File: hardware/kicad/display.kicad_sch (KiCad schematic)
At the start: 0 parts

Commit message: first pass schematic and new fpc symbol
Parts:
- added C31, C32, C33, C34, C35, C36, C37, C38, C39, C40: 1u, symbol Device:C_Small
- added C41: 4.7u, symbol Device:C_Small
- added D4, D5, D6: MBR0530, Diode_SMD:D_SOD-123, symbol Diode:MBR0530
- added L5: 10u 1A, symbol Device:L
- added Q7: SI1308EDL, Package_TO_SOT_SMD:SOT-23, symbol Transistor_FET:AO3400A
- added R17: 0.47, Resistor_SMD:R_0402_1005Metric, symbol Device:R_Small
- added R17: 1M, Resistor_SMD:R_0402_1005Metric, symbol Device:R_Small
- added U8: FPC-05FB-24PH20, symbol plantpal:GDEW0154M10
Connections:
- new net: C32.2, U8.5 (VGH)
- new net: C38.2, U8.24 (VCOM)
- new net: C34.2, U8.18 (VDD)
- new net: C41.2, D6.2 (A), L5.2, Q7.3 (D)
- new net: C36.2, U8.22 (VSL)
- new net: C35.2, U8.20 (VSH)
- new net: C41.1, D4.1 (K), D5.2 (A)
- new net: C31.1, U8.4 (VGL)
- new net +3V3: C33.2, C40.1, L5.1, U8.15 (VDDIO), U8.16 (VCI)
- new net BUSY: U8.9 (BUSY)
- new net CS: U8.12 (CS)
- new net DC: U8.11 (D/C)
- new net GDR: Q7.1 (G), R17.2, U8.2 (GDR)
- new net GND: C31.2, C32.1, C33.1, C34.1, C35.1, C36.1, C37.1, C38.1, C39.1, C40.2, D5.1 (K), R17.1, R17.1, U8.17 (VSS), U8.8 (BS1)
- new net PREVGH: C39.2, D6.1 (K), U8.21 (PREVGH)
- new net PREVGL: C37.2, D4.2 (A), U8.23 (PREVGL)
- new net RESE: Q7.2 (S), R17.2, U8.3 (RESE)
- new net RST: U8.10 (RST)
- new net SCLK: U8.13 (SCLK)
- new net SDI: U8.14 (SDI)
- new net TSCL: U8.6 (TSCL)
- new net TSDA: U8.7 (TSDA)
- no-connect marks 0 -> 1
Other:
- note added: "Display Manufacturer: Good Display Part Number: GDEW0154I9FC 26Pin FPC, 0.5mm Pitch, 0.25mm Pad Size Pin 1 and 26 are not used No connector is need, soldered directly to board Use 24 pin FPC connector footprint for debugging"
- note added: "E-Paper Display"
- note added: "Sheets Connection"

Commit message: clean-up
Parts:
- C41: value 4.7u -> 4u7
- renumbered C34 to C32, C38 to C33, C36 to C34, C37 to C36, C31 to C37, C32 to C38, C33 to C39, C39 to C40, C40 to C42, U8 to J4
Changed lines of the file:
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@@
   (symbol (lib_id "Device:C_Small") (at 64.77 38.735 270) (mirror x) (unit 1)
     (in_bom yes) (on_board yes) (dnp no)
-    (property "Reference" "C32" (at 66.04 41.275 90)
+    (property "Reference" "C38" (at 66.04 41.275 90)
       (effects (font (size 1.27 1.27)) (justify left))
     )
@@
       (project "plantpal"
         (path "/59b4123e-c7be-466b-a5db-658b8f0c1171/3265fc00-478b-4188-a908-4fc9b1aaf6ab"
-          (reference "C32") (unit 1)
+          (reference "C38") (unit 1)
         )
       )
@@
   (symbol (lib_id "Device:C_Small") (at 55.88 109.855 270) (unit 1)
     (in_bom yes) (on_board yes) (dnp no)
-    (property "Reference" "C38" (at 57.15 108.585 90)
+    (property "Reference" "C33" (at 57.15 108.585 90)
       (effects (font (size 1.27 1.27)) (justify left))
     )
@@
       (project "plantpal"
         (path "/59b4123e-c7be-466b-a5db-658b8f0c1171/3265fc00-478b-4188-a908-4fc9b1aaf6ab"
-          (reference "C38") (unit 1)
+          (reference "C33") (unit 1)
         )
       )
@@
         )
         (path "/59b4123e-c7be-466b-a5db-658b8f0c1171/3265fc00-478b-4188-a908-4fc9b1aaf6ab"
-          (reference "#PWR089") (unit 1)
+          (reference "#PWR0102") (unit 1)
         )
       )
@@
   (symbol (lib_id "power:GND") (at 69.85 113.665 0) (mirror y) (unit 1)
     (in_bom yes) (on_board yes) (dnp no) (fields_autoplaced)
-    (property "Reference" "#PWR092" (at 69.85 120.015 0)
+    (property "Reference" "#PWR095" (at 69.85 120.015 0)
       (effects (font (size 1.27 1.27)) hide)
     )
@@
       (project "plantpal"
         (path "/59b4123e-c7be-466b-a5db-658b8f0c1171/3265fc00-478b-4188-a908-4fc9b1aaf6ab"
-          (reference "#PWR092") (unit 1)
+          (reference "#PWR095") (unit 1)
         )
       )
@@
         )
         (path "/59b4123e-c7be-466b-a5db-658b8f0c1171/3265fc00-478b-4188-a908-4fc9b1aaf6ab"
-          (reference "R26") (unit 1)
+          (reference "R25") (unit 1)
         )
       )
@@
         )
         (path "/59b4123e-c7be-466b-a5db-658b8f0c1171/3265fc00-478b-4188-a908-4fc9b1aaf6ab"
-          (reference "#PWR091") (unit 1)
+          (reference "#PWR094") (unit 1)
         )
       )
@@
   (symbol (lib_id "Device:C_Small") (at 177.8 59.055 0) (mirror y) (unit 1)
     (in_bom yes) (on_board yes) (dnp no)
-    (property "Reference" "C40" (at 175.26 57.15 0)
+    (property "Reference" "C42" (at 175.26 57.15 0)
       (effects (font (size 1.27 1.27)) (justify left))
     )
@@
       (project "plantpal"
         (path "/59b4123e-c7be-466b-a5db-658b8f0c1171/3265fc00-478b-4188-a908-4fc9b1aaf6ab"
-          (reference "C40") (unit 1)
+          (reference "C42") (unit 1)
         )
       )
@@
   (symbol (lib_id "Device:C_Small") (at 54.61 86.995 270) (unit 1)
     (in_bom yes) (on_board yes) (dnp no)
-    (property "Reference" "C34" (at 55.88 85.725 90)
+    (property "Reference" "C32" (at 55.88 85.725 90)
       (effects (font (size 1.27 1.27)) (justify left))
     )
@@
       (project "plantpal"
         (path "/59b4123e-c7be-466b-a5db-658b8f0c1171/3265fc00-478b-4188-a908-4fc9b1aaf6ab"
-          (reference "C34") (unit 1)
+          (reference "C32") (unit 1)
         )
       )
@@
   (symbol (lib_id "power:GND") (at 177.8 65.405 0) (mirror y) (unit 1)
     (in_bom yes) (on_board yes) (dnp no) (fields_autoplaced)
-    (property "Reference" "#PWR097" (at 177.8 71.755 0)
+    (property "Reference" "#PWR0101" (at 177.8 71.755 0)
       (effects (font (size 1.27 1.27)) hide)
     )
@@
       (project "plantpal"
         (path "/59b4123e-c7be-466b-a5db-658b8f0c1171/3265fc00-478b-4188-a908-4fc9b1aaf6ab"
-          (reference "#PWR097") (unit 1)
+          (reference "#PWR0101") (unit 1)
         )
       )
@@
   (symbol (lib_id "Device:C_Small") (at 63.5 106.045 270) (unit 1)
     (in_bom yes) (on_board yes) (dnp no)
-    (property "Reference" "C37" (at 64.77 104.775 90)
+    (property "Reference" "C36" (at 64.77 104.775 90)
       (effects (font (size 1.27 1.27)) (justify left))
     )
@@
       (project "plantpal"
         (path "/59b4123e-c7be-466b-a5db-658b8f0c1171/3265fc00-478b-4188-a908-4fc9b1aaf6ab"
-          (reference "C37") (unit 1)
+          (reference "C36") (unit 1)
         )
       )
@@
   (symbol (lib_id "Device:C_Small") (at 109.22 61.595 0) (mirror x) (unit 1)
     (in_bom yes) (on_board yes) (dnp no)
-    (property "Reference" "C39" (at 102.87 59.055 0)
+    (property "Reference" "C40" (at 102.87 59.055 0)
       (effects (font (size 1.27 1.27)) (justify left))
     )
@@
       (project "plantpal"
         (path "/59b4123e-c7be-466b-a5db-658b8f0c1171/3265fc00-478b-4188-a908-4fc9b1aaf6ab"
-          (reference "C39") (unit 1)
+          (reference "C40") (unit 1)
         )
       )
@@
   (symbol (lib_id "Device:C_Small") (at 57.15 102.235 270) (unit 1)
     (in_bom yes) (on_board yes) (dnp no)
-    (property "Reference" "C36" (at 58.42 100.965 90)
+    (property "Reference" "C34" (at 58.42 100.965 90)
       (effects (font (size 1.27 1.27)) (justify left))
     )
@@
       (project "plantpal"
         (path "/59b4123e-c7be-466b-a5db-658b8f0c1171/3265fc00-478b-4188-a908-4fc9b1aaf6ab"
-          (reference "C36") (unit 1)
+          (reference "C34") (unit 1)
         )
       )
@@
   (symbol (lib_id "power:GND") (at 146.05 80.645 0) (mirror y) (unit 1)
     (in_bom yes) (on_board yes) (dnp no) (fields_autoplaced)
-    (property "Reference" "#PWR095" (at 146.05 86.995 0)
+    (property "Reference" "#PWR099" (at 146.05 86.995 0)
       (effects (font (size 1.27 1.27)) hide)
     )
@@
       (project "plantpal"
         (path "/59b4123e-c7be-466b-a5db-658b8f0c1171/3265fc00-478b-4188-a908-4fc9b1aaf6ab"
-          (reference "#PWR095") (unit 1)
+          (reference "#PWR099") (unit 1)
         )
       )
@@
   (symbol (lib_id "power:GND") (at 74.93 45.085 0) (mirror y) (unit 1)
     (in_bom yes) (on_board yes) (dnp no) (fields_autoplaced)
-    (property "Reference" "#PWR090" (at 74.93 51.435 0)
+    (property "Reference" "#PWR096" (at 74.93 51.435 0)
       (effects (font (size 1.27 1.27)) hide)
     )
@@
       (project "plantpal"
         (path "/59b4123e-c7be-466b-a5db-658b8f0c1171/3265fc00-478b-4188-a908-4fc9b1aaf6ab"
-          (reference "#PWR090") (unit 1)
+          (reference "#PWR096") (unit 1)
         )
       )
@@
       (effects (font (size 1.27 1.27)) (justify left))
     )
-    (property "Value" "4.7u" (at 132.715 48.26 0)
+    (property "Value" "4u7" (at 132.715 48.26 0)
       (effects (font (size 1.27 1.27)) (justify left))
     )
@@
         )
         (path "/59b4123e-c7be-466b-a5db-658b8f0c1171/3265fc00-478b-4188-a908-4fc9b1aaf6ab"
-          (reference "#PWR096") (unit 1)
+          (reference "#PWR0100") (unit 1)
         )
       )
@@
         )
         (path "/59b4123e-c7be-466b-a5db-658b8f0c1171/3265fc00-478b-4188-a908-4fc9b1aaf6ab"
-          (reference "R25") (unit 1)
+          (reference "R26") (unit 1)
         )
       )
@@
   (symbol (lib_id "Device:C_Small") (at 69.85 79.375 180) (unit 1)
     (in_bom yes) (on_board yes) (dnp no)
-    (property "Reference" "C33" (at 76.2 76.835 0)
+    (property "Reference" "C39" (at 76.2 76.835 0)
       (effects (font (size 1.27 1.27)) (justify left))
     )
@@
       (project "plantpal"
         (path "/59b4123e-c7be-466b-a5db-658b8f0c1171/3265fc00-478b-4188-a908-4fc9b1aaf6ab"
-          (reference "C33") (unit 1)
+          (reference "C39") (unit 1)
         )
       )
@@
   (symbol (lib_id "plantpal:GDEW0154M10") (at 34.29 62.865 0) (mirror y) (unit 1)
     (in_bom yes) (on_board yes) (dnp no)
-    (property "Reference" "U8" (at 26.67 116.84 0)
+    (property "Reference" "J4" (at 26.67 116.84 0)
       (effects (font (size 1.27 1.27)) (justify left))
     )
@@
     )
     (property "Part Number" "FPC-05FB-24PH20" (at 34.29 62.865 0)
+      (effects (font (size 1.27 1.27)) hide)
+    )
+    (property "Part Description" "" (at 34.29 62.865 0)
+      (effects (font (size 1.27 1.27)) hide)
+    )
+    (property "Manufacturer Part Number" "" (at 34.29 62.865 0)
+      (effects (font (size 1.27 1.27)) hide)
+    )
+    (property "Distributor" "" (at 34.29 62.865 0)
+      (effects (font (size 1.27 1.27)) hide)
+    )
+    (property "Distributor Part Number" "" (at 34.29 62.865 0)
+      (effects (font (size 1.27 1.27)) hide)
+    )
+    (property "Distributor Link" "" (at 34.29 62.865 0)
       (effects (font (size 1.27 1.27)) hide)
     )
@@
       (project "plantpal"
         (path "/59b4123e-c7be-466b-a5db-658b8f0c1171/3265fc00-478b-4188-a908-4fc9b1aaf6ab"
-          (reference "U8") (unit 1)
+          (reference "J4") (unit 1)
         )
       )
@@
   (symbol (lib_id "power:GND") (at 109.22 42.545 0) (mirror y) (unit 1)
     (in_bom yes) (on_board yes) (dnp no) (fields_autoplaced)
-    (property "Reference" "#PWR094" (at 109.22 48.895 0)
+    (property "Reference" "#PWR097" (at 109.22 48.895 0)
       (effects (font (size 1.27 1.27)) hide)
     )
@@
       (project "plantpal"
         (path "/59b4123e-c7be-466b-a5db-658b8f0c1171/3265fc00-478b-4188-a908-4fc9b1aaf6ab"
-          (reference "#PWR094") (unit 1)
+          (reference "#PWR097") (unit 1)
         )
       )
@@
   (symbol (lib_id "Device:C_Small") (at 64.77 33.655 90) (unit 1)
     (in_bom yes) (on_board yes) (dnp no)
-    (property "Reference" "C31" (at 69.85 31.115 90)
+    (property "Reference" "C37" (at 69.85 31.115 90)
       (effects (font (size 1.27 1.27)) (justify left))
     )
@@
       (project "plantpal"
         (path "/59b4123e-c7be-466b-a5db-658b8f0c1171/3265fc00-478b-4188-a908-4fc9b1aaf6ab"
-          (reference "C31") (unit 1)
-        )
-      )
+          (reference "C37") (unit 1)
+        )
+      )

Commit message: clean-up
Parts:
- R17: value 0.47 -> 470m
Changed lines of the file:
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@@
       (effects (font (size 1.27 1.27)))
     )
-    (property "Value" "0.47" (at 141.605 74.295 0)
+    (property "Value" "470m" (at 141.605 74.295 0)
       (effects (font (size 1.27 1.27)))
     )

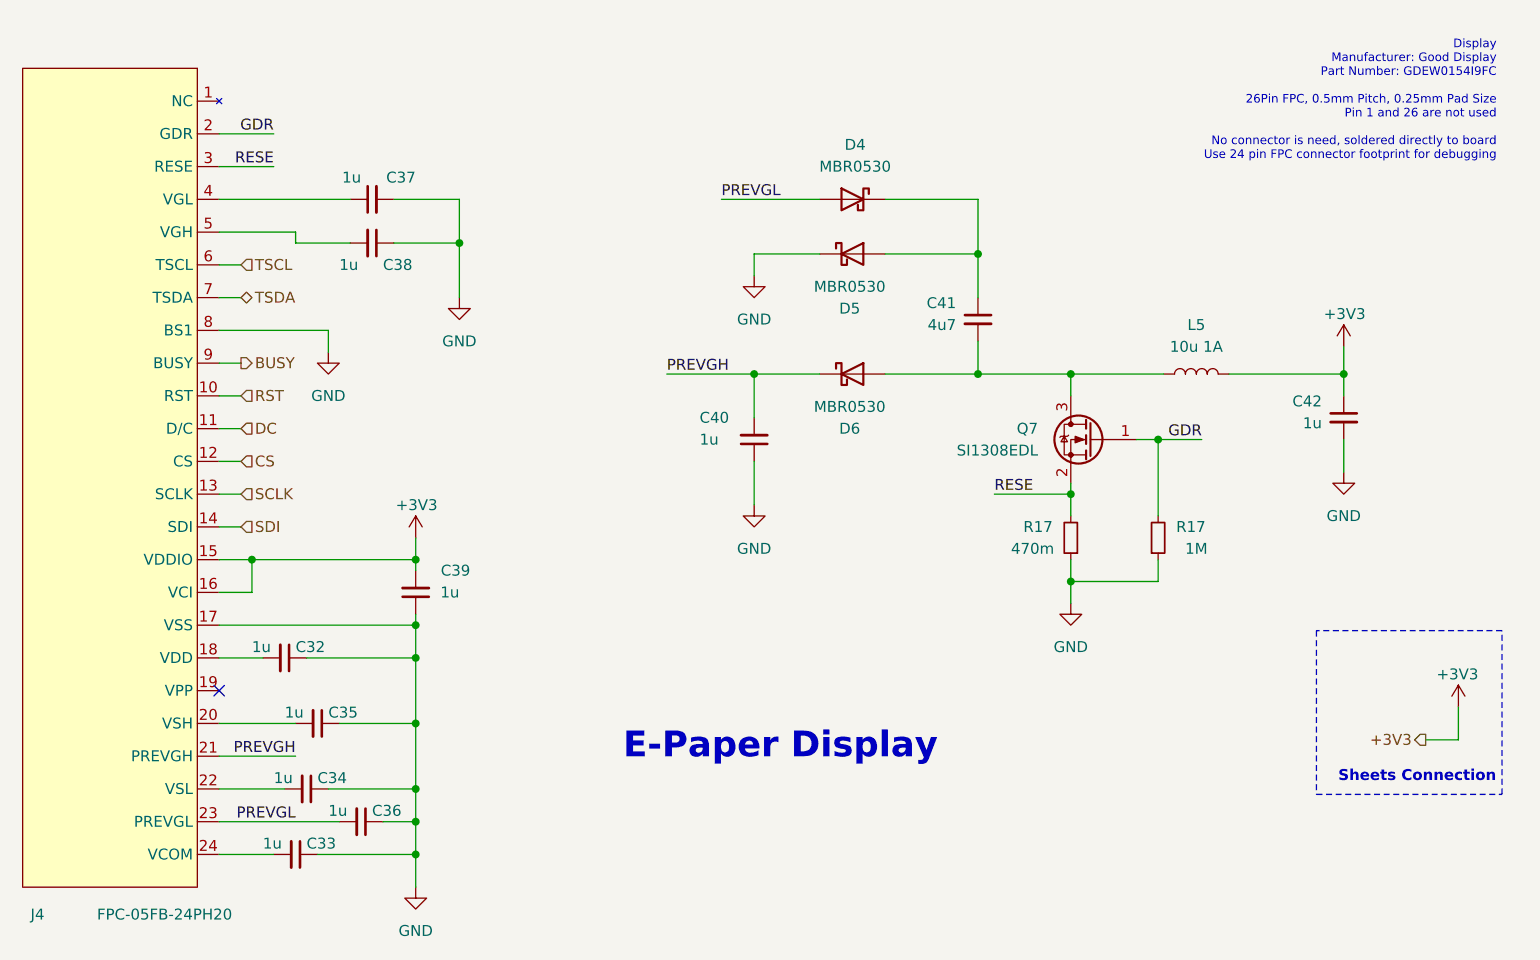
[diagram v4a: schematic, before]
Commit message: change resistor to 0402
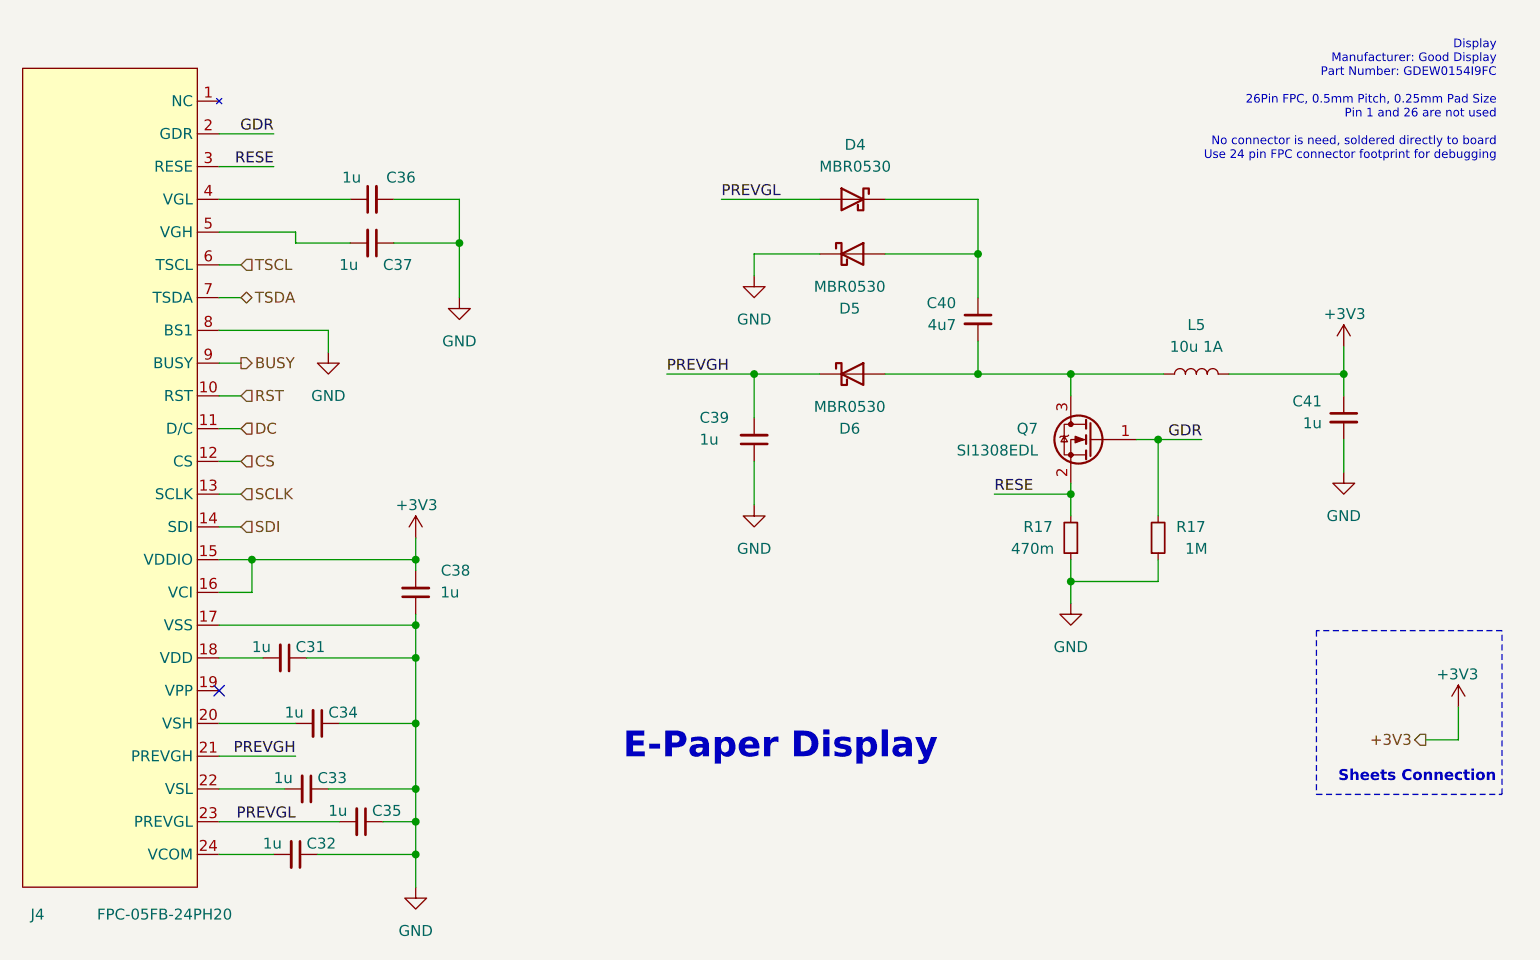
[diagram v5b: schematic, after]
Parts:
- renumbered C32 to C31, C33 to C32, C34 to C33, C35 to C34, C36 to C35, C37 to C36, C38 to C37, C39 to C38, C40 to C39, C41 to C40, C42 to C41

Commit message: update note
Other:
- note added: "Display Manufacturer: Good Display Part Number: GDEW0154I9FC Non-flex Alternative: GDEW0154M10 26Pin FPC, 0.5mm Pitch, 0.25mm Pad Size Pin 1 and 26 are not used No connector is need, soldered directly to board Use 24 pin FPC connector footprint for debugging"
- note removed: "Display Manufacturer: Good Display Part Number: GDEW0154I9FC 26Pin FPC, 0.5mm Pitch, 0.25mm Pad Size Pin 1 and 26 are not used No connector is need, soldered directly to board Use 24 pin FPC connector footprint for debugging"
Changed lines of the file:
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@@
     (effects (font (size 1.27 1.27) (thickness 0.6) bold) (justify left bottom))
   )
-  (text "Display \nManufacturer: Good Display\nPart Number: GDEW0154I9FC\n\n26Pin FPC, 0.5mm Pitch, 0.25mm Pad Size\nPin 1 and 26 are not used \n\nNo connector is need, soldered directly to board\nUse 24 pin FPC connector footprint for debugging"
+  (text "Display \nManufacturer: Good Display\nPart Number: GDEW0154I9FC\nNon-flex Alternative: GDEW0154M10\n\n26Pin FPC, 0.5mm Pitch, 0.25mm Pad Size\nPin 1 and 26 are not used \n\nNo connector is need, soldered directly to board\nUse 24 pin FPC connector footprint for debugging"
     (at 195.58 29.21 0)
     (effects (font (size 1 1)) (justify right bottom))
